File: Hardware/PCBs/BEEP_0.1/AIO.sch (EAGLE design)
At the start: 74 parts, among them IC1 ULN2803ASOP18, IC2 ULN2803ASOP18, IC3 74HC238D, IC4 74HC238D, U2 TB6612FNG, U3 ATXMEGA64D3-AU, X10 MICROMATCH-10, X2 MICROMATCH-8, X3 MICROMATCH-8, X4 MICROMATCH-8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

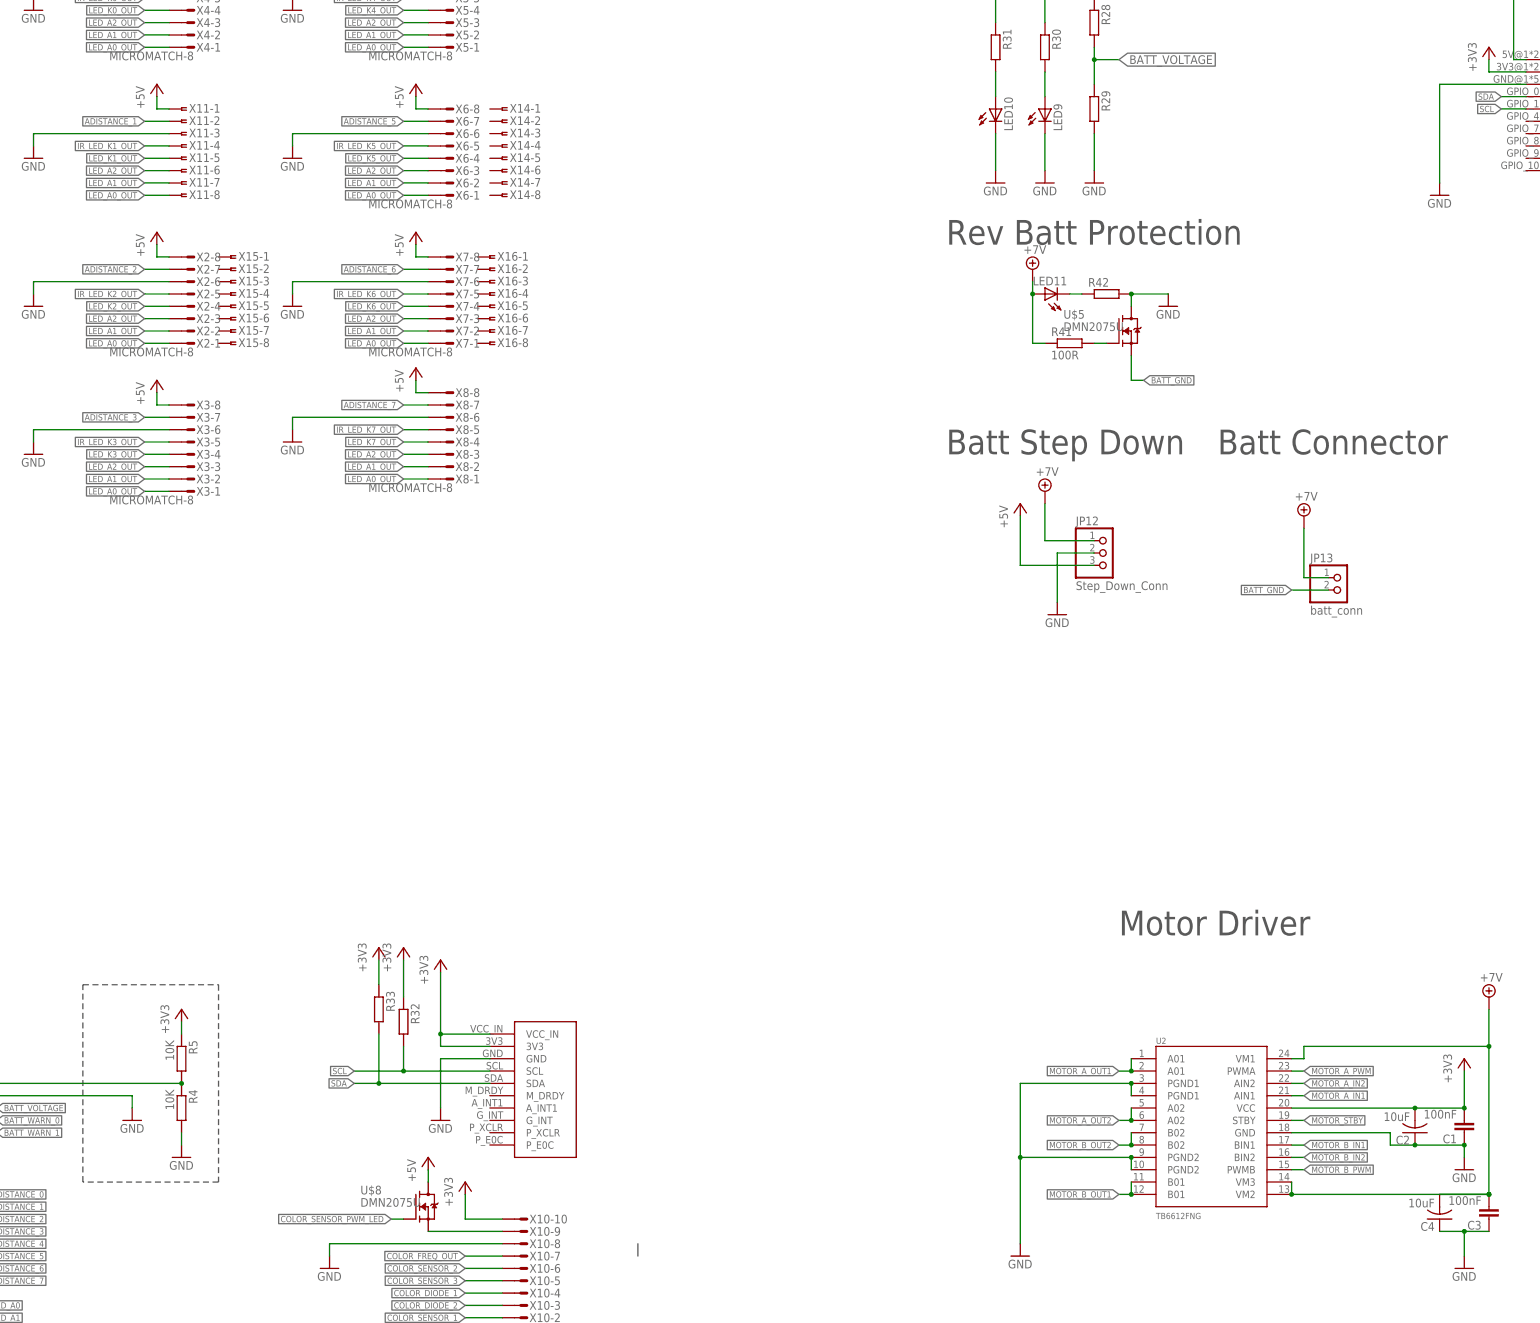
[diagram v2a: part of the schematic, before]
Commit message: continue routing add hardware architecture shematic
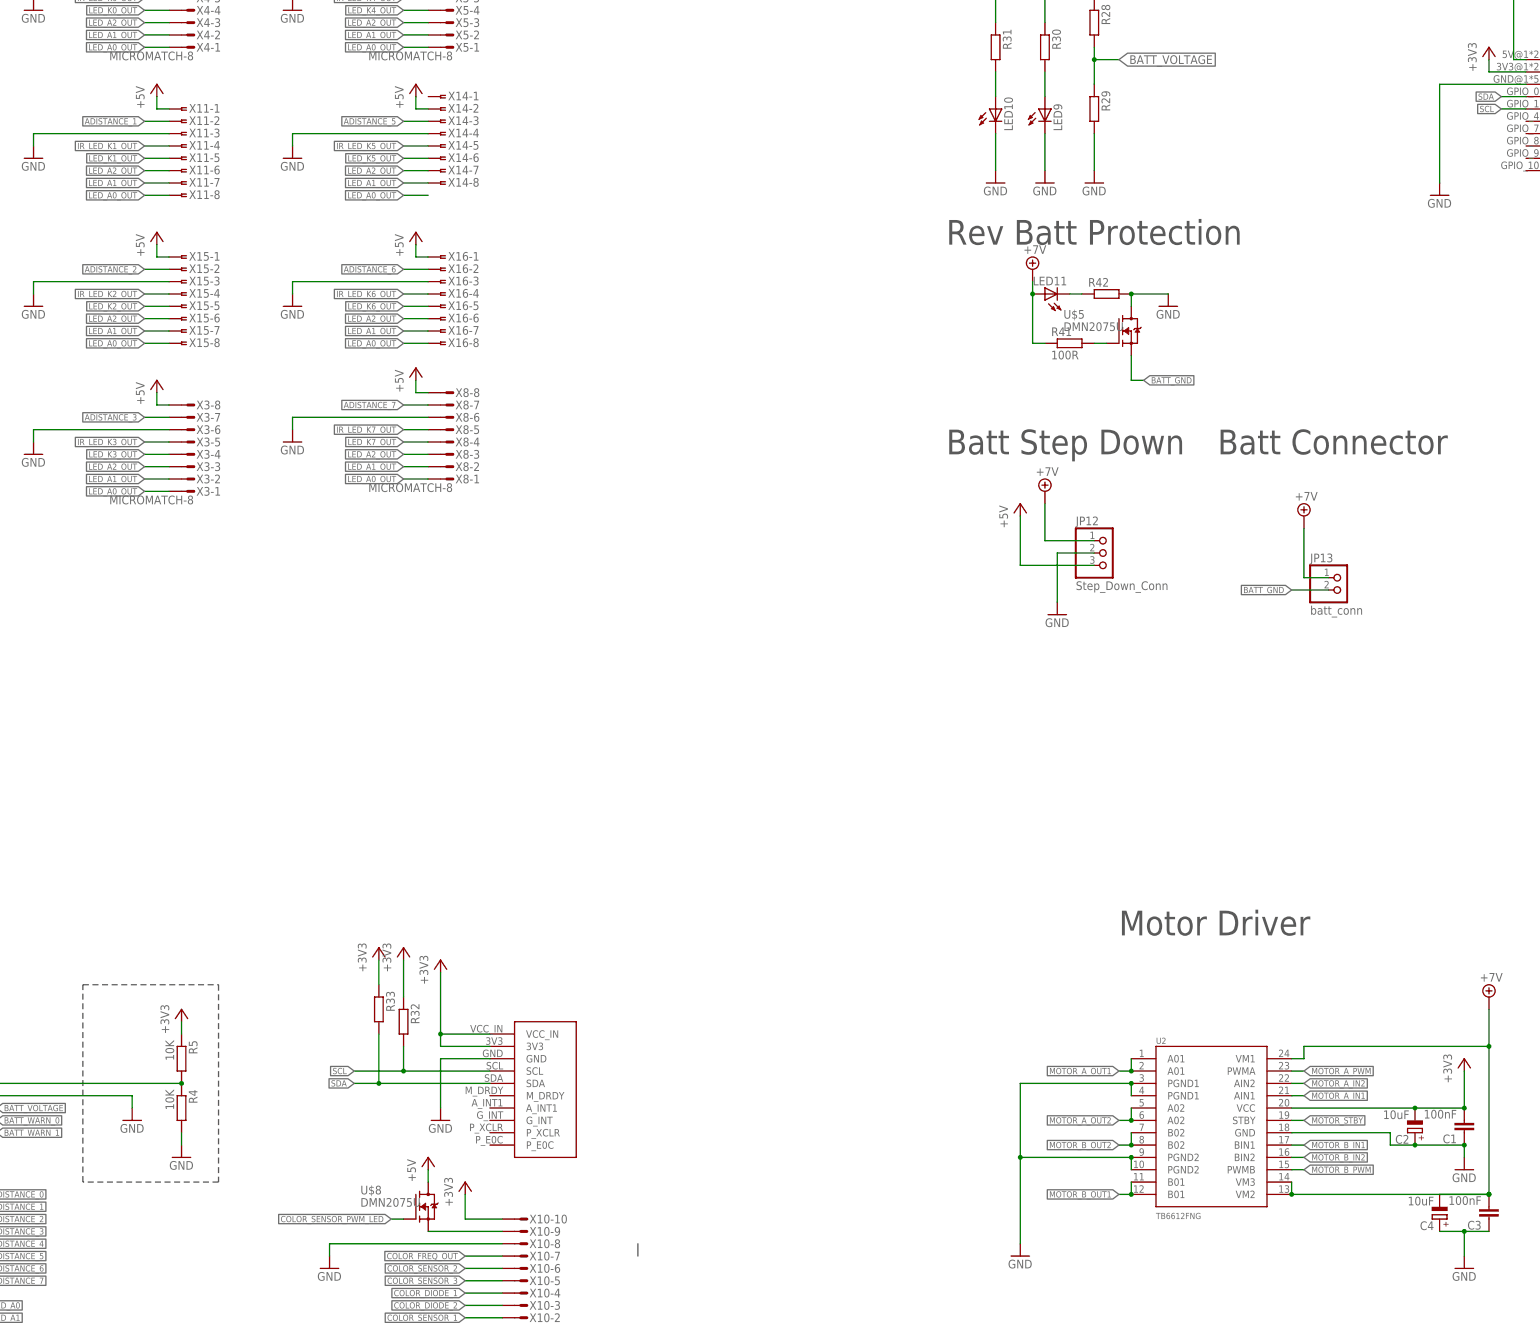
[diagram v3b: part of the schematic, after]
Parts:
- removed X2, X6, X7: MICROMATCH-8, Con-amp-micromatch:MICROMATCH-8
- C2, C4: device rcl:C-USC1812 -> rcl:CPOL-EUSMCD
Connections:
- net +3V3: now also C2.-; no longer C2.2
- net +5V: now also X14-2.1, X15-1.1, X16-1.1; no longer X2-8.S, X6-8.S, X7-8.S
- net +7V: now also C4.-; no longer C4.2
- net ADISTANCE_2: now also X15-2.1; no longer X2-7.S
- net ADISTANCE_5: now also X14-3.1; no longer X6-7.S
- net ADISTANCE_6: now also X16-2.1; no longer X7-7.S
- net GND: now also C2.+, C4.+, X14-4.1, X15-3.1, X16-3.1; no longer C2.1, C4.1, X2-6.S, X6-6.S, X7-6.S
- net IR_LED_K2_OUT: now also X15-4.1; no longer X2-5.S
- net IR_LED_K5_OUT: now also X14-5.1; no longer X6-5.S
- net IR_LED_K6_OUT: now also X16-4.1; no longer X7-5.S
- net LED_A0_OUT: now also X15-8.1, X16-8.1; no longer X2-1.S, X6-1.S, X7-1.S
- net LED_A1_OUT: now also X14-8.1, X15-7.1, X16-7.1; no longer X2-2.S, X6-2.S, X7-2.S
- net LED_A2_OUT: now also X14-7.1, X15-6.1, X16-6.1; no longer X2-3.S, X6-3.S, X7-3.S
- net LED_K2_OUT: now also X15-5.1; no longer X2-4.S
- net LED_K5_OUT: now also X14-6.1; no longer X6-4.S
- net LED_K6_OUT: now also X16-5.1; no longer X7-4.S
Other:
- moved on the sheet: X14-1, X14-2, X14-3, X14-4, X14-5, X14-6, X14-7, X14-8, X15-1, X15-2, X15-3, X15-4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

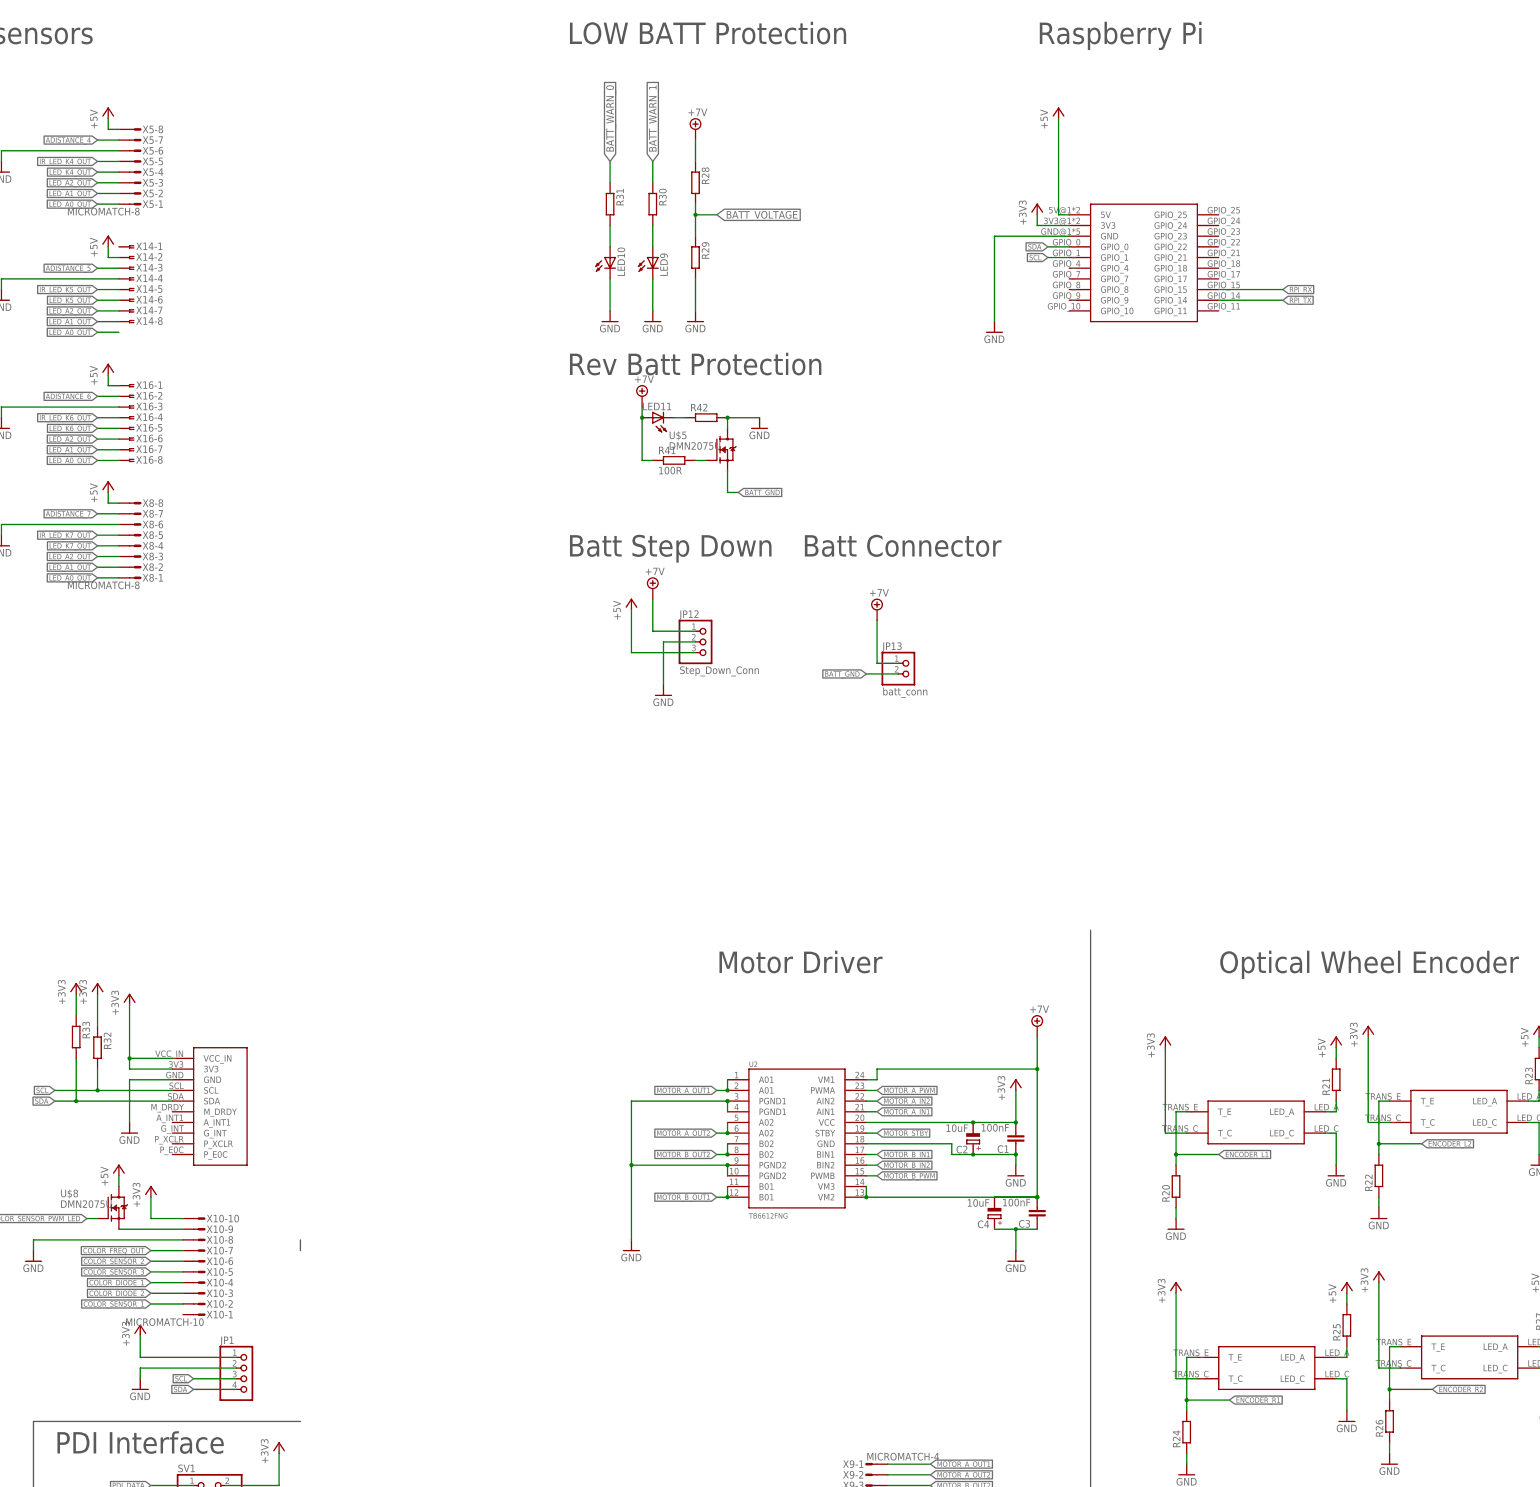
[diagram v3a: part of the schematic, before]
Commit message: add momentary push button with mosfet latch circuit as on/off switch continue routing
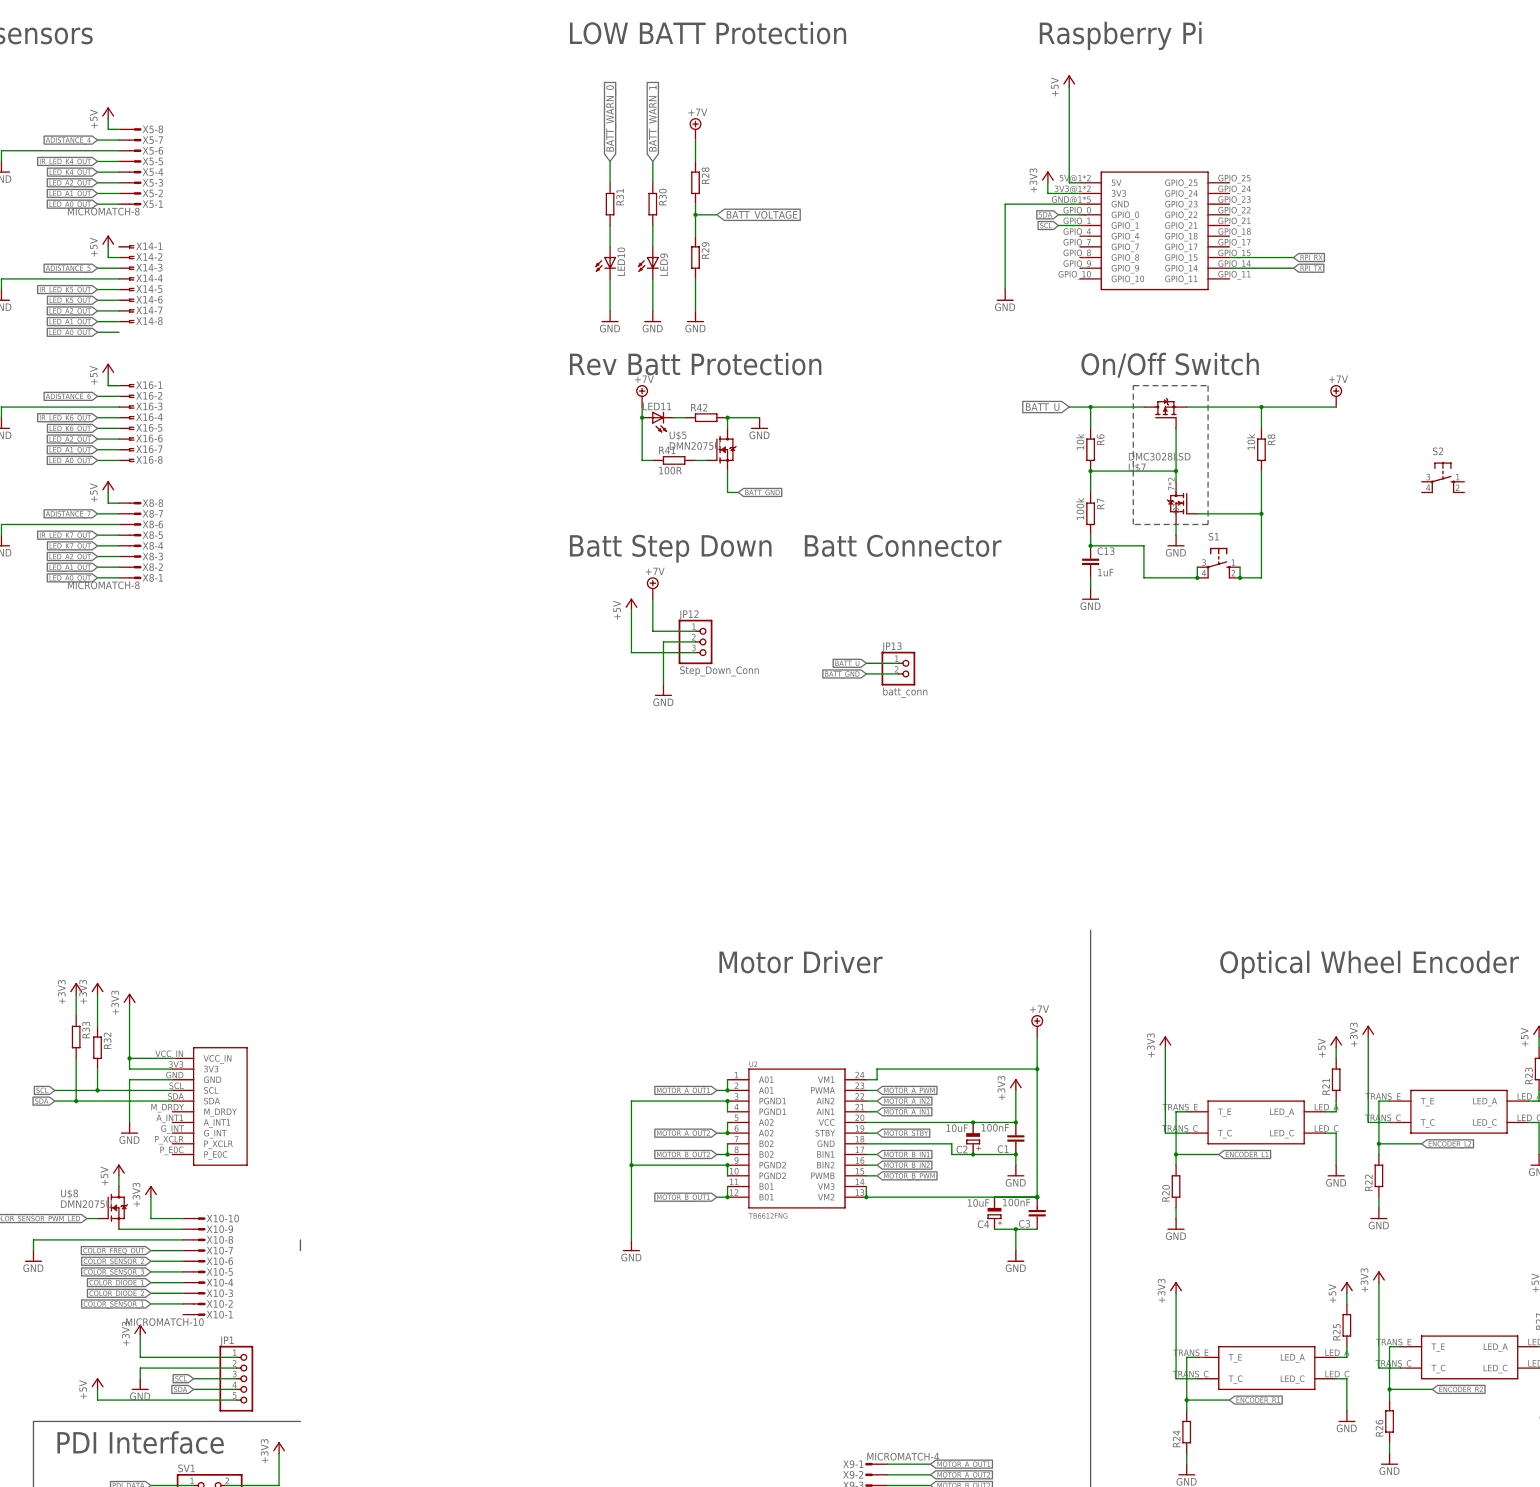
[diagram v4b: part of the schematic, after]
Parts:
- added C13: 1uF, rcl:C-EUC0603
- added R6, R8: 10k, rcl:R-EU_R0603
- added R7: 100k, rcl:R-EU_R0603
- added S1, S2: (no value), switch-omron:10-XX
- added U$7: DMC3028LSD, BEEP:DMC3028LSD
- JP1: device pinhead:PINHD-1X4 -> pinhead:PINHD-1X5
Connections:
- new net BATT_U: JP13.1, R6.1, U$7.D2
- new net N$16: C13.1, R7.2, S1.P, S1.P1
- new net N$18: R8.2, S1.S, S1.S1, U$7.G1
- new net N$22: R6.2, R7.1, U$7.D1, U$7.G2
- net +5V: now also JP1.5
- net +7V: now also R8.1, U$7.S2; no longer JP13.1
- net GND: now also C13.2, U$7.S1
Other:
- note added: "On/Off Switch"

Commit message: continue routing replace so16 multiplexer with ssop16 add ssop16 footprint to beep library
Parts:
- added U$10, U$11, U$12, U$13, U$14, U$15, U$16, U$9: DMN2075U, BEEP:DMN2075U
- IC3, IC4: value 74HC238D -> 74HC238SSOP; device BEEP:74HC238D -> BEEP:74HC238SSOP
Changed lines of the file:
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@@
 <part name="GND14" library="supply1" deviceset="GND" device=""/>
 <part name="C10" library="rcl" deviceset="C-EU" device="C0603" value="100nF"/>
-<part name="IC3" library="BEEP" deviceset="74HC238" device="D"/>
+<part name="IC3" library="BEEP" deviceset="74HC238" device="SSOP" value="74HC238SSOP"/>
 <part name="GND16" library="supply1" deviceset="GND" device=""/>
 <part name="+3V3" library="supply1" deviceset="+3V3" device=""/>
-<part name="IC4" library="BEEP" deviceset="74HC238" device="D"/>
+<part name="IC4" library="BEEP" deviceset="74HC238" device="SSOP" value="74HC238SSOP"/>
 <part name="GND17" library="supply1" deviceset="GND" device=""/>
 <part name="+3V4" library="supply1" deviceset="+3V3" device=""/>
@@
 <part name="SUPPLY2" library="supply2" deviceset="+7V" device=""/>
 <part name="S2" library="switch-omron" deviceset="10-XX" device=""/>
+<part name="U$9" library="BEEP" deviceset="DMN2075U" device=""/>
+<part name="U$10" library="BEEP" deviceset="DMN2075U" device=""/>
+<part name="U$11" library="BEEP" deviceset="DMN2075U" device=""/>
+<part name="U$12" library="BEEP" deviceset="DMN2075U" device=""/>
+<part name="U$13" library="BEEP" deviceset="DMN2075U" device=""/>
+<part name="U$14" library="BEEP" deviceset="DMN2075U" device=""/>
+<part name="U$15" library="BEEP" deviceset="DMN2075U" device=""/>
+<part name="U$16" library="BEEP" deviceset="DMN2075U" device=""/>
 </parts>
 <sheets>
@@
 <instance part="SUPPLY2" gate="G$1" x="515.62" y="327.66"/>
 <instance part="S2" gate="1" x="541.02" y="307.34" rot="R270"/>
+<instance part="U$9" gate="G$1" x="535.94" y="406.4"/>
+<instance part="U$10" gate="G$1" x="535.94" y="393.7"/>
+<instance part="U$11" gate="G$1" x="535.94" y="381"/>
+<instance part="U$12" gate="G$1" x="535.94" y="368.3"/>
+<instance part="U$13" gate="G$1" x="535.94" y="355.6"/>
+<instance part="U$14" gate="G$1" x="535.94" y="342.9"/>
+<instance part="U$15" gate="G$1" x="546.1" y="340.36"/>
+<instance part="U$16" gate="G$1" x="546.1" y="355.6"/>
 </instances>
 <busses>
